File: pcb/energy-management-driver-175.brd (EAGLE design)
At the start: 151.4 x 32.9 mm, 49 parts, among them T1 BT138-V, T2 BT138-V, T3 BT138-V, T4 BT138-V, T5 BT138-V, T6 BT138-V, T7 BT138-V, T8 BT138-V

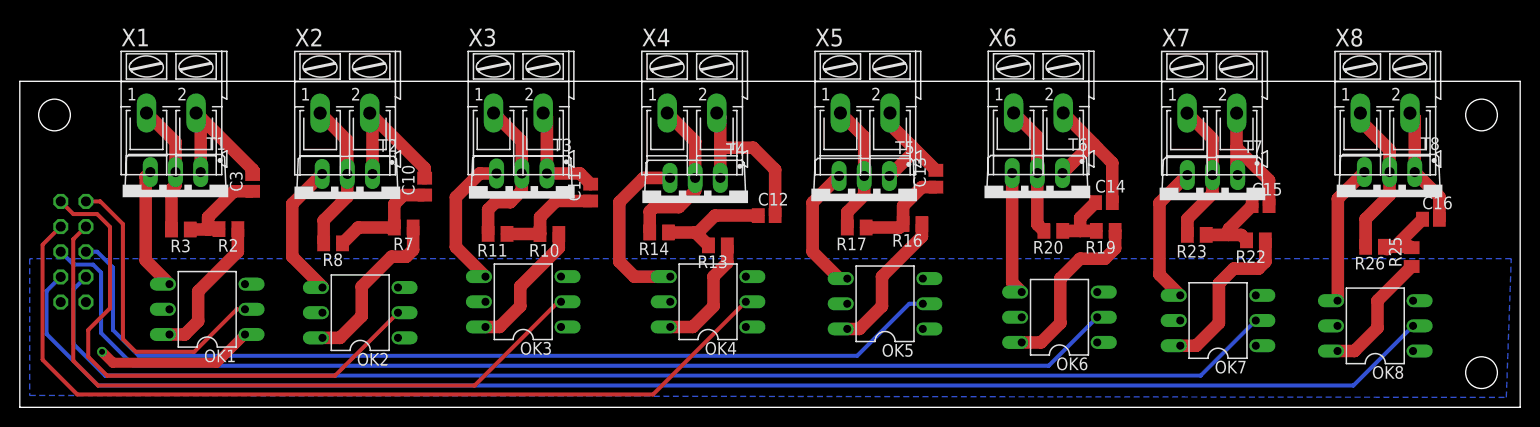
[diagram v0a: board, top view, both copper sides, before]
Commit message: updated driver board and add input board
Update driver 175 board to use skun terminal. Also add input board for
hotel asia
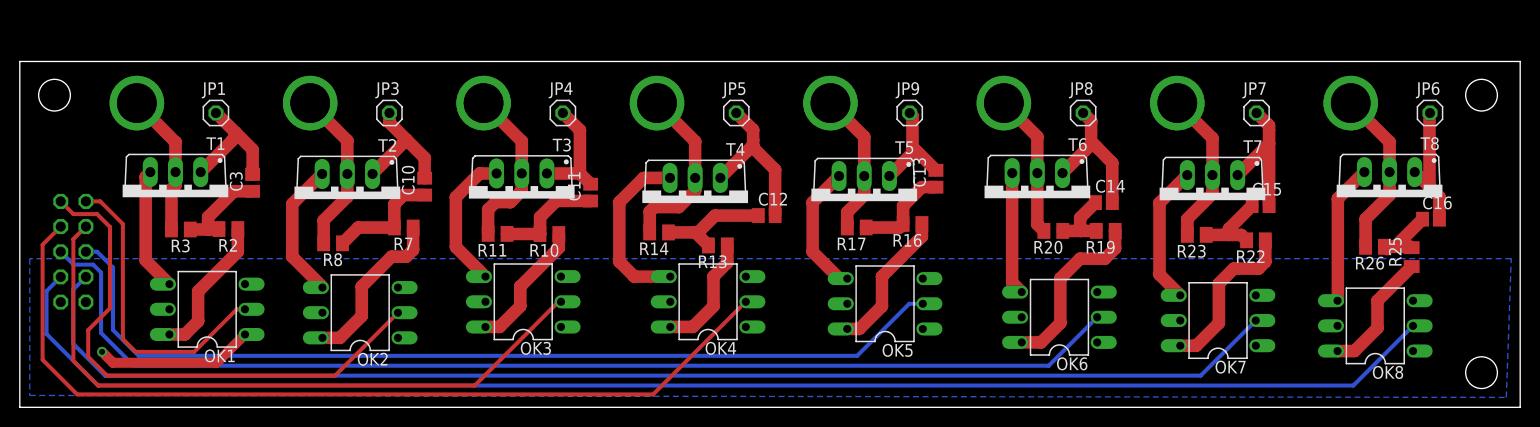
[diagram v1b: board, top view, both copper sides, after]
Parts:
- removed X1, X2, X3, X4, X5, X6, X7, X8: (no value), con-ptr500:AK300/2
- added JP1, JP3, JP4, JP5, JP6, JP7, JP8, JP9: (no value), pinhead:1X01
- added U$1, U$2, U$3, U$4, U$5, U$6, U$7, U$8: CONN-SKUN, bontor:CONN-SKUN
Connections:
- net N$15: now also JP3.1; no longer X2.2
- net N$21: now also JP4.1; no longer X3.2
- net N$27: now also JP5.1; no longer X4.2
- net N$33: now also JP9.1; no longer X5.2
- net N$39: now also JP8.1; no longer X6.2
- net N$45: now also JP7.1; no longer X7.2
- net N$51: now also JP6.1; no longer X8.2
- net N$52: now also U$2.P$2; no longer X2.1
- net N$53: now also U$3.P$2; no longer X3.1
- net N$54: now also U$4.P$2; no longer X4.1
- net N$55: now also U$5.P$2; no longer X8.1
- net N$56: now also U$6.P$2; no longer X7.1
- net N$57: now also U$7.P$2; no longer X6.1
- net N$58: now also U$8.P$2; no longer X5.1
- net N$6: now also JP1.1; no longer X1.2
- net N$9: now also U$1.P$2; no longer X1.1
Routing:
- net N$15: track 15.1 -> 12.9 mm
- net N$54: track 16.6 -> 18.0 mm, vias 0 -> 1
- net N$52: track 15.3 -> 16.7 mm, vias 0 -> 1
- net N$56: track 14.8 -> 16.2 mm, vias 0 -> 1
- net N$58: track 13.3 -> 14.7 mm, vias 0 -> 1
- net N$53: track 15.7 -> 17.1 mm, vias 0 -> 1
- net N$55: track 15.7 -> 17.1 mm, vias 0 -> 1
- net N$9: track 13.3 -> 14.7 mm, vias 0 -> 1
- net N$57: track 13.2 -> 14.6 mm, vias 0 -> 1
- net N$51: track 11.9 -> 13.3 mm
- net N$27: track 17.8 -> 16.7 mm
- net N$6: track 14.7 -> 13.6 mm
- net N$45: track 13.5 -> 14.5 mm
- net N$39: track 15.5 -> 14.5 mm
- net N$33: track 11.6 -> 10.8 mm
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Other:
- board size 151.4 x 32.9 mm -> 151.4 x 34.9 mm
